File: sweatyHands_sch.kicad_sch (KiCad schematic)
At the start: 21 parts, among them J1 USB_C_Receptacle_USB2.0_16P, J2 Conn_01x04_Socket, Q1 UMH3N, SW1 SW_SPST, U1 ESP32-WROOM-32E, U2 USBLC6-2SC6, U3 CP2104, U4 LM1117LD-3.3

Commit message: .
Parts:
- added C11, C13, C4, C7, C8: 22u, symbol Device:C_Small
- added C12, C14, C5, C9: 100n, symbol Device:C_Small
- added C6: 4u7, symbol Device:C_Small
- added R10, R6, R8, R9: 1K, symbol Device:R_Small
- added R11, R12: 4K7, symbol Device:R_Small
- added R14, R3, R7: 10K, symbol Device:R_Small
- added R4, R5: 22R, symbol Device:R_Small
- C2: value 22u -> 100n
- C3: value 22u -> 4u7
- U4: value LM1117LD-3.3 -> TLV1117LV-3.3
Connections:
- net +5V: now also U2.5 (VBUS), U4.2 (VI), U4.3 (VI), U4.4 (VI), C7.1
- net GND: now also C1.2, C2.2, C3.2, D2.1 (K), H1.1, H2.1, H3.1, H4.1, J2.1 (Pin_1), SW1.1 (A), U3.2 (GND), U3.25 (GND), C11.2, C12.2, C13.2, C14.2, C4.2, C5.2, C6.2, C7.2, C8.2, C9.2
- net at D1.1 (RK): now also R8.2
- net at D1.2 (GK): now also R9.2
- net at D1.3 (BK): now also R10.2
- net +3.3V: now reaches D1.4 (A)
- net +3.3V: now also J2.2 (Pin_2), U1.2 (VDD), U4.5 (VO), U4.6 (VO), U4.7 (VO), U4.9 (VO), C11.1, C12.1, C13.1, C8.1, R11.1, R12.1, R14.1, R6.1, R7.1
- net at U3.16 (VPP): now also C6.1
- net RTS: now reaches U3.19 (~{RTS})
- net RTS: now also Q1.2 (B1), Q1.3 (C2)
- net at U3.20 (RXD): now also R5.1
- net at U3.21 (TXD): now also R4.1
- net DTR: now reaches U3.23 (~{DTR})
- net DTR: now also Q1.1 (E1), Q1.5 (B2)
- net +3.3VA: now reaches U3.5 (VIO)
- net +3.3VA: now also U3.6 (VDD), C4.1, C5.1, R3.1
- net at U3.9 (~{RST}): now also R3.2
- net at D2.2 (A): now also R6.2
- net IO0: now reaches U1.25 (IO0)
- net IO0: now also Q1.6 (C1)
- net EN: now reaches U1.3 (EN)
- net EN: now also Q1.4 (E2), C14.1, R14.2
- net SW: now reaches SW1.2 (B)
- net SW: now also C9.1, R7.2
- net SDA: now reaches J2.3 (Pin_3)
- net SDA: now also R12.2
- net SCL: now reaches J2.4 (Pin_4)
- net SCL: now also R11.2
- new net LED_B: R10.1
- new net LED_G: R9.1
- new net LED_R: R8.1
- new net RX: R4.2
- new net TX: R5.2
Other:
- note added: "GND"
- note added: "SCL"
- note added: "SDA"
- note added: "SWIIC"
- note added: "VCC"
- moved on the sheet: D1, D2, Q1A, Q1B, U4

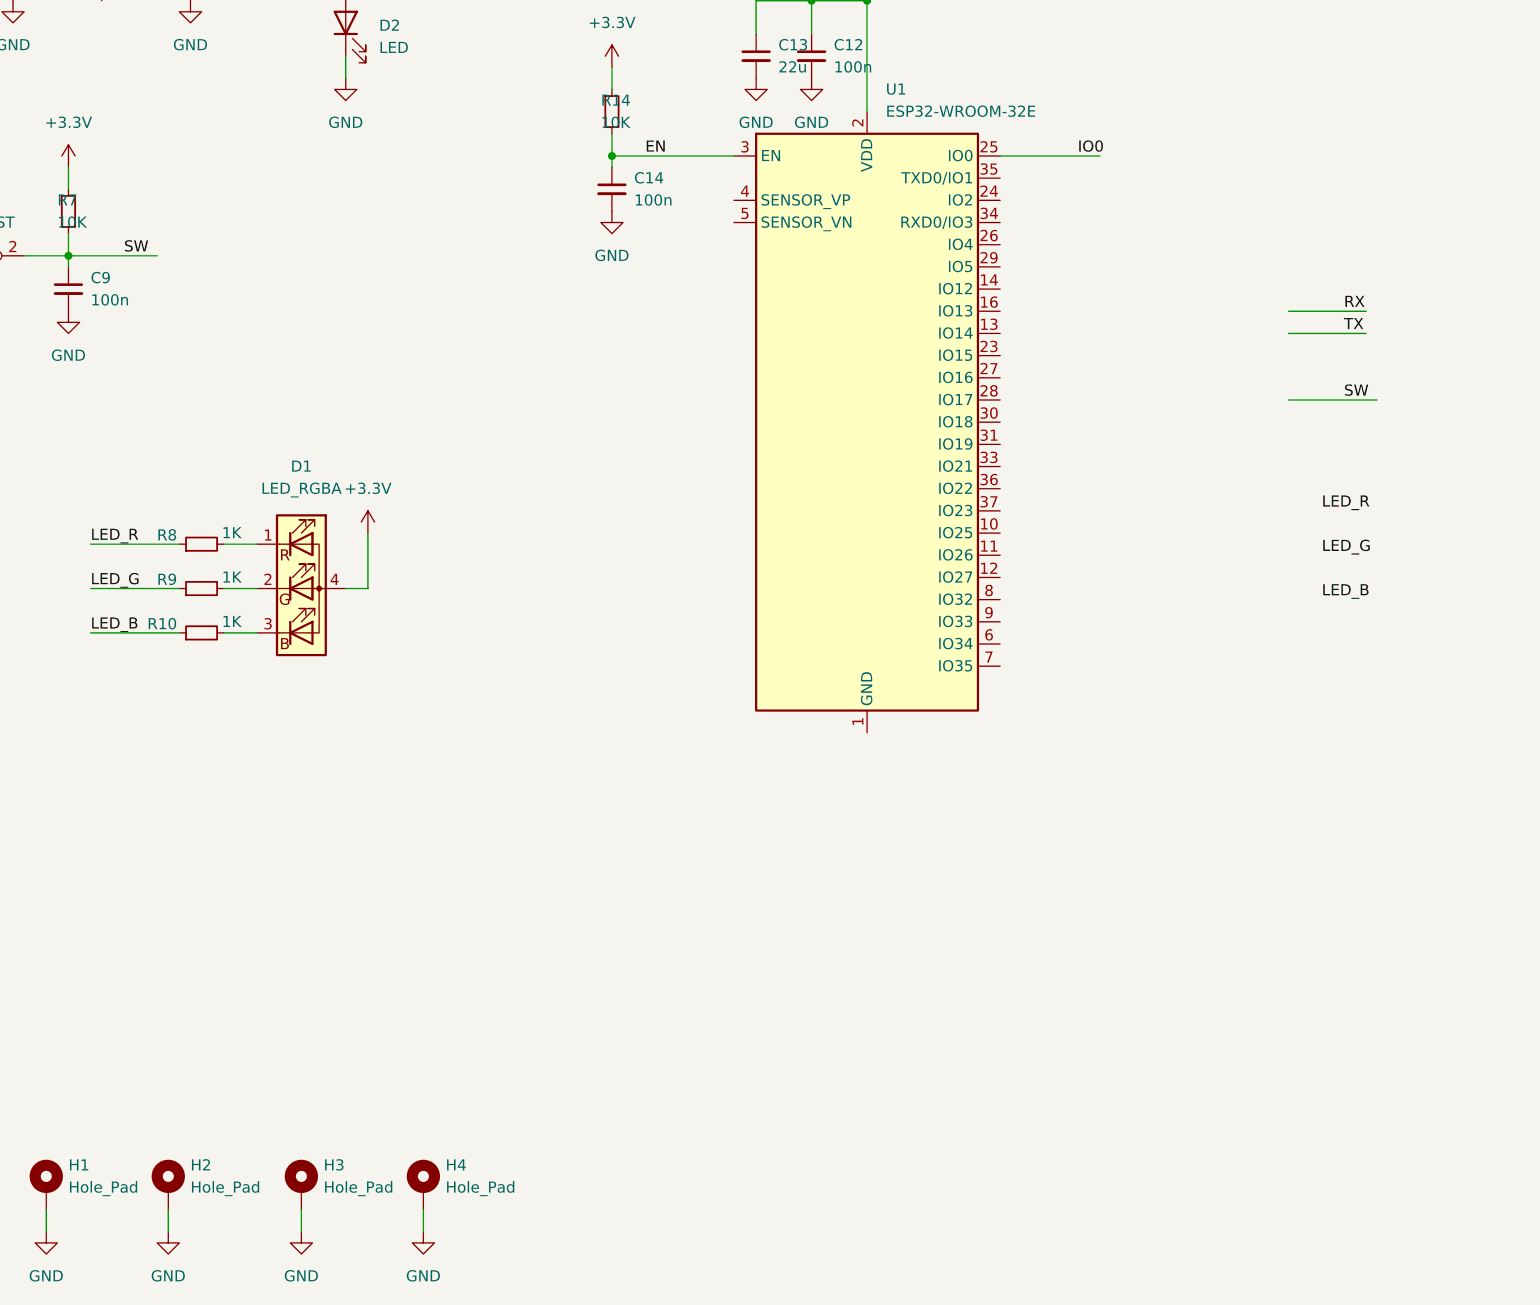
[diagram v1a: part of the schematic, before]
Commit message: Finished power and MCU
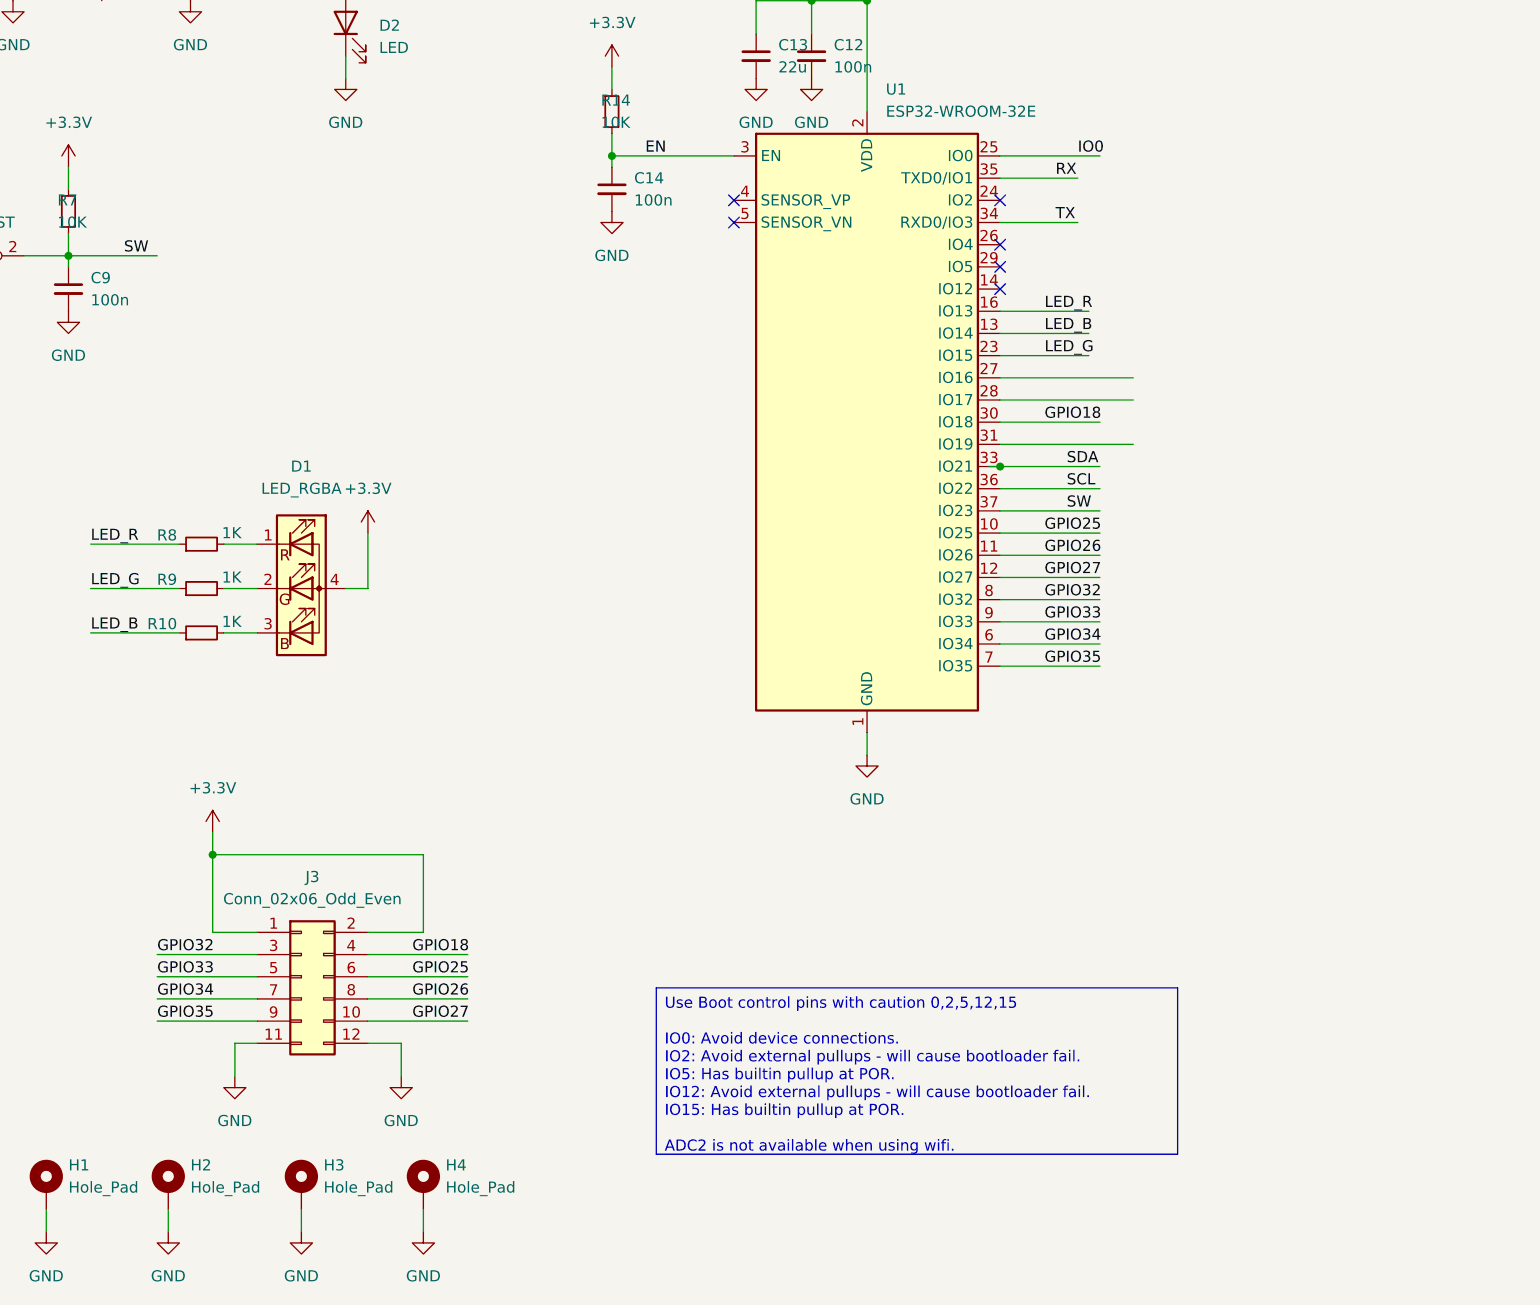
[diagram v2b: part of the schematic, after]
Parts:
- added J3: Conn_02x06_Odd_Even, symbol Connector_Generic:Conn_02x06_Odd_Even
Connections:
- net +3.3V: now also J3.1 (Pin_1), J3.2 (Pin_2)
- net GND: now also U1.1 (GND), U1.15 (GND), U1.38 (GND), U1.39 (GND), J3.11 (Pin_11), J3.12 (Pin_12)
- net LED_B: now also U1.13 (IO14)
- net LED_G: now also U1.23 (IO15)
- net LED_R: now also U1.16 (IO13)
- net RX: now also U1.35 (TXD0/IO1)
- net SCL: now also U1.36 (IO22)
- net SDA: now also U1.33 (IO21)
- net SW: now also U1.37 (IO23)
- net TX: now also U1.34 (RXD0/IO3)
- net GPIO25: now reaches U1.10 (IO25)
- net GPIO25: now also J3.6 (Pin_6)
- net GPIO26: now reaches U1.11 (IO26)
- net GPIO26: now also J3.8 (Pin_8)
- net GPIO27: now reaches U1.12 (IO27)
- net GPIO27: now also J3.10 (Pin_10)
- net GPIO18: now reaches U1.30 (IO18)
- net GPIO18: now also J3.4 (Pin_4)
- net GPIO34: now reaches U1.6 (IO34)
- net GPIO34: now also J3.7 (Pin_7)
- net GPIO35: now reaches U1.7 (IO35)
- net GPIO35: now also J3.9 (Pin_9)
- net GPIO32: now reaches U1.8 (IO32)
- net GPIO32: now also J3.3 (Pin_3)
- net GPIO33: now reaches U1.9 (IO33)
- net GPIO33: now also J3.5 (Pin_5)
- no-connect marks 0 -> 6

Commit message: Added Duel Power
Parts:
- removed C1, C4: 22u, symbol Device:C_Small
- removed C2, C5: 100n, symbol Device:C_Small
- removed C3, C6: 4u7, symbol Device:C_Small
- removed F1: Polyfuse 1A, symbol Device:Polyfuse_Small
- removed FB1: MPZ2012S221AT000, symbol Device:FerriteBead_Small
- removed J1: USB_C_Receptacle_USB2.0_16P, symbol Connector:USB_C_Receptacle_USB2.0_16P
- removed R1, R2: 5k1, symbol Device:R_Small
- removed R3: 10K, symbol Device:R_Small
- removed R4, R5: 22R, symbol Device:R_Small
- removed U2: USBLC6-2SC6, Package_TO_SOT_SMD:SOT-23-6, symbol Power_Protection:USBLC6-2SC6
- removed U3: CP2104, Package_DFN_QFN:QFN-24-1EP_4x4mm_P0.5mm_EP2.6x2.6mm, symbol Interface_USB:CP2104
- added 47K: 1K, symbol Device:R_Small
- added C10, C18, C22, C23: 22u, symbol Device:C_Small
- added C15, C19: 100n, symbol Device:C_Small
- added C16, C17: 4u7, symbol Device:C_Small
- added C20: 10u, symbol Device:C_Small
- added C21: 0.1u, symbol Device:C_Small
- added C24: 75p, symbol Device:C_Small
- added D3: PESD5V0S1UL_315, PESD5V0S1UL_315:DIO_PESD5V0S1UL_315, symbol PESD5V0S1UL_315:PESD5V0S1UL_315
- added D4: SS34, Diode_SMD:D_SMA, symbol Diode:SS34
- added F2: Polyfuse 500ma, symbol Device:Polyfuse_Small
- added F3: Polyfuse 1.2-1.5A hold, symbol Device:Polyfuse_Small
- added FB2, FB3: MPZ2012S221AT000, symbol Device:FerriteBead_Small
- added J4: Barrel_Jack, symbol Connector:Barrel_Jack
- added J5: USB_C_Receptacle_USB2.0_16P, symbol Connector:USB_C_Receptacle_USB2.0_16P
- added L1: 15u, symbol Device:L
- added R13, R22: 100K, symbol Device:R_Small
- added R15: 59K 1%, symbol Device:R_Small
- added R16: 10K, symbol Device:R_Small
- added R17, R18: 22R, symbol Device:R_Small
- added R19, R20: 5k1, symbol Device:R_Small
- added R21: 49.9R, symbol Device:R_Small
- added R23: 13.3K, symbol Device:R_Small
- added U2: TPS54202DDCT, TPS54202DDCT:SOT95P280X110-6N, symbol TPS54202DDCT:TPS54202DDCT
- added U5: TPS2116DRL, Package_TO_SOT_SMD:SOT-583-8, symbol Power_Management:TPS2116DRL
- added U6: TPS2553DBVR, TPS2553DBVR:SOT95P280X145-6N, symbol TPS2553DBVR:TPS2553DBVR
- added U7: CP2104, Package_DFN_QFN:QFN-24-1EP_4x4mm_P0.5mm_EP2.6x2.6mm, symbol Interface_USB:CP2104
- added U8: USBLC6-2SC6, Package_TO_SOT_SMD:SOT-23-6, symbol Power_Protection:USBLC6-2SC6
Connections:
- net +3.3V: now also 47K.1
- net +3.3VA: now also C18.1, C19.1, R16.1, U7.5 (VIO), U7.6 (VDD)
- net +5V: now also C10.1, C15.1, C17.1, U5.2 (VOUT), U5.7 (VOUT), U7.7 (REGIN), U7.8 (VBUS), U8.5 (VBUS)
- net DTR: now also U7.23 (~{DTR})
- net GND: now also J3.9 (Pin_9), C10.2, C15.2, C16.2, C17.2, C18.2, C19.2, C20.2, C22.2, C23.2, C24.2, J5.A1 (GND), J5.A12 (GND), J5.B1 (GND), J5.B12 (GND), J5.S1 (SHIELD), R15.2, R19.1, R20.1, R23.2, U2.1 (GND), U2.4 (FB), U6.2 (GND), U7.2 (GND), U7.25 (GND), U8.2 (GND)
- net RTS: now also U7.19 (~{RTS})
- net RX: now also R17.2
- net TX: now also R18.2
- net GPIO35 renamed FAULT
- net FAULT: now also 47K.2, U6.4 (~{FAULT}); no longer J3.9 (Pin_9)
- new net: C16.1, U7.16 (VPP)
- new net: R18.1, U7.20 (RXD)
- new net: R17.1, U7.21 (TXD)
- new net: U7.3 (D+), U8.6 (I/O1)
- new net: U7.4 (D-), U8.1 (I/O1)
- new net: R16.2, U7.9 (~{RST})
- new net: D3.A, J5.A4 (VBUS), J5.A9 (VBUS), J5.B4 (VBUS), J5.B9 (VBUS)
- new net: D3.K, F2.1
- new net: C24.1, R21.2, R22.1
- new net: R22.2, R23.1
- new net: FB3.1, U5.3 (VIN1)
- new net: D4.1 (K), F3.1
- new net: C20.1, F3.2, U2.3 (VIN)
- new net: F2.2, R13.1, U6.1 (IN)
- new net: J5.A5 (CC1), R19.2
- new net: C21.2, L1.1, U2.2 (SW)
- new net: C21.1, U2.6 (BOOT)
- new net: J5.A6 (D+), J5.B6 (D+), U8.4 (I/O2)
- new net: J5.A7 (D-), J5.B7 (D-), U8.3 (I/O2)
- new net: J5.B5 (CC2), R20.2
- new net: FB2.1, U6.6 (OUT)
- new net: FB2.2, U5.6 (VIN2)
- new net: D4.2 (A), J4.1
- new net: R13.2, U6.3 (EN)
- new net: R15.1, U6.5 (ILIM)
- new net Vout: C22.1, C23.1, FB3.2, L1.2, R21.1
- no-connect marks 6 -> 7
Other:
- moved on the sheet: C11, C12, C13, C14, C7, C8, C9, D2, J2, J3, Q1A, Q1B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

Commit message: .
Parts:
- added J7: Conn_01x02_Socket, Connector:Banana_Jack_2Pin, symbol Connector:Conn_01x02_Socket
- added Q2: 2N2222, 2N2222:TO127P580H530-3, symbol 2N2222:2N2222
- added Q3, Q6: AO3400A, Package_TO_SOT_SMD:SOT-23, symbol Transistor_FET:AO3400A
- added Q4, Q5: DMG2305UX-13, DMG2305UX-13:SOT91P240X110-3N, symbol DMG2305UX-13:DMG2305UX-13
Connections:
- net GND: now also J4.2
- net GPIO16: now reaches U1.27 (IO16)
- net GPIO17: now reaches U1.28 (IO17)
- net GPIO19: now reaches U1.31 (IO19)
- new net: J7.2 (Pin_2), Q3.3 (D), Q4.2
- new net: J7.1 (Pin_1), Q5.2, Q6.3 (D)
